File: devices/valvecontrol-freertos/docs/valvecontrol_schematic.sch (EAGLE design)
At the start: 38 parts, among them J1 M12-4PIN, J2 M12-4PIN, J3 PWR-3PIN, SW1 TACTILE, U1 nRF52832-QFAA, U2 RFM95C, U3 MCP2515-I/SO, U4 SN65HVD230DR, U5 FM25V02-G, U6 W25Q16JVSSIQ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

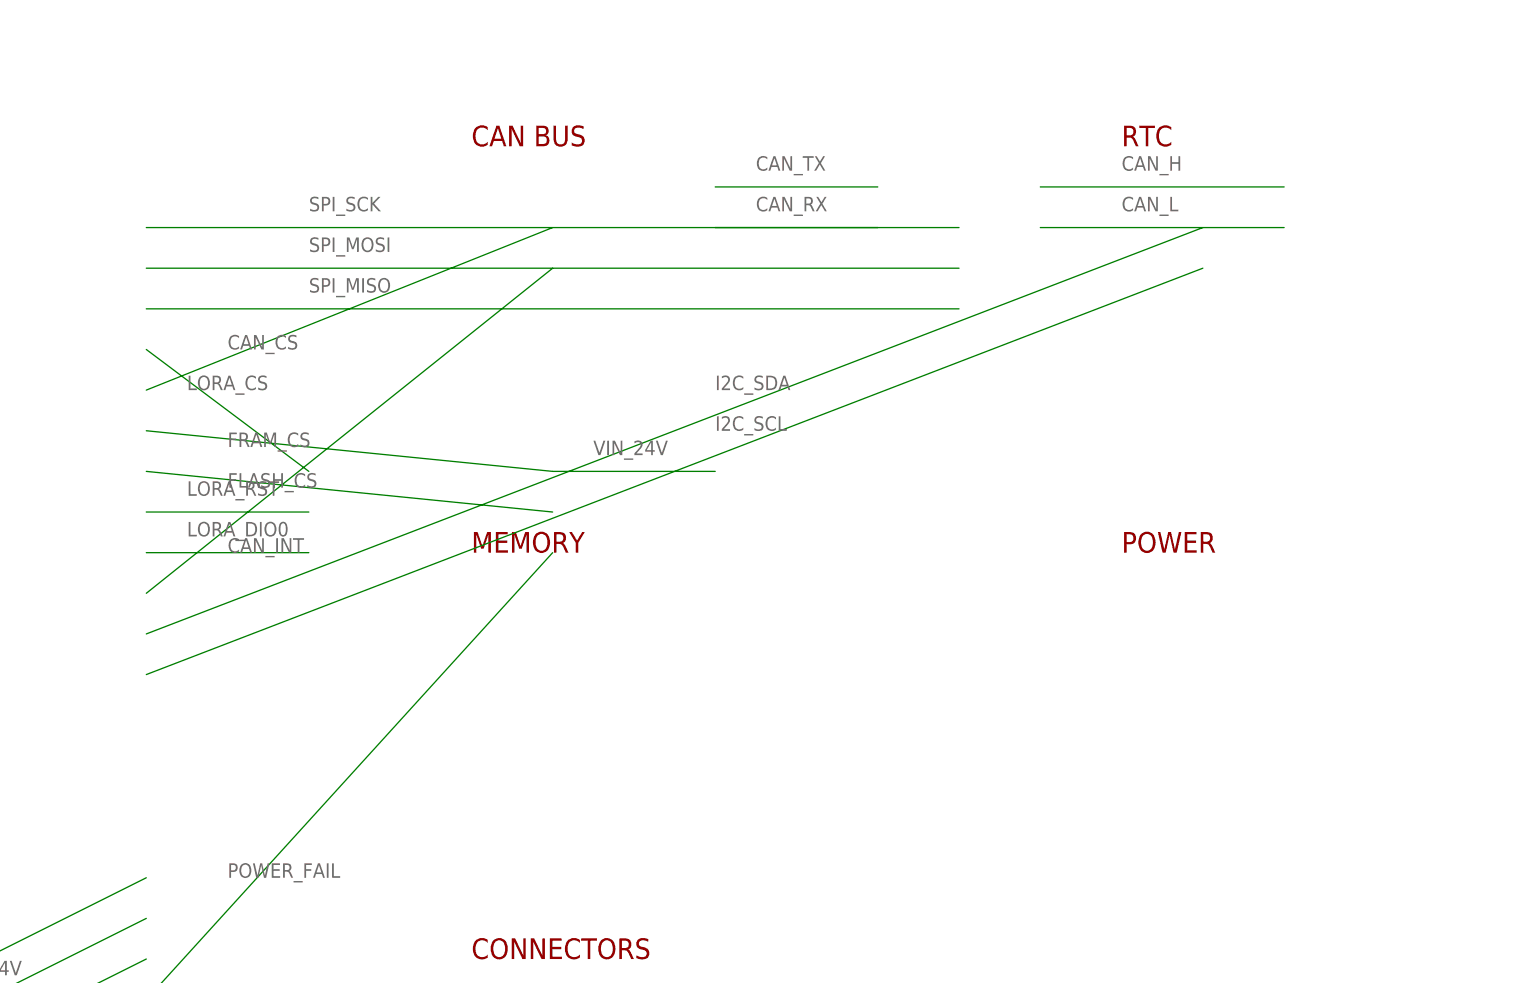
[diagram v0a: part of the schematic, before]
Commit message: So many little fixes to schematics, to board_config.h, to OTA, to flash ram, to moving logging back to FRAM device, to looking at how to make the devices last for 10+ years, to making sure BLE is integrated correctly.
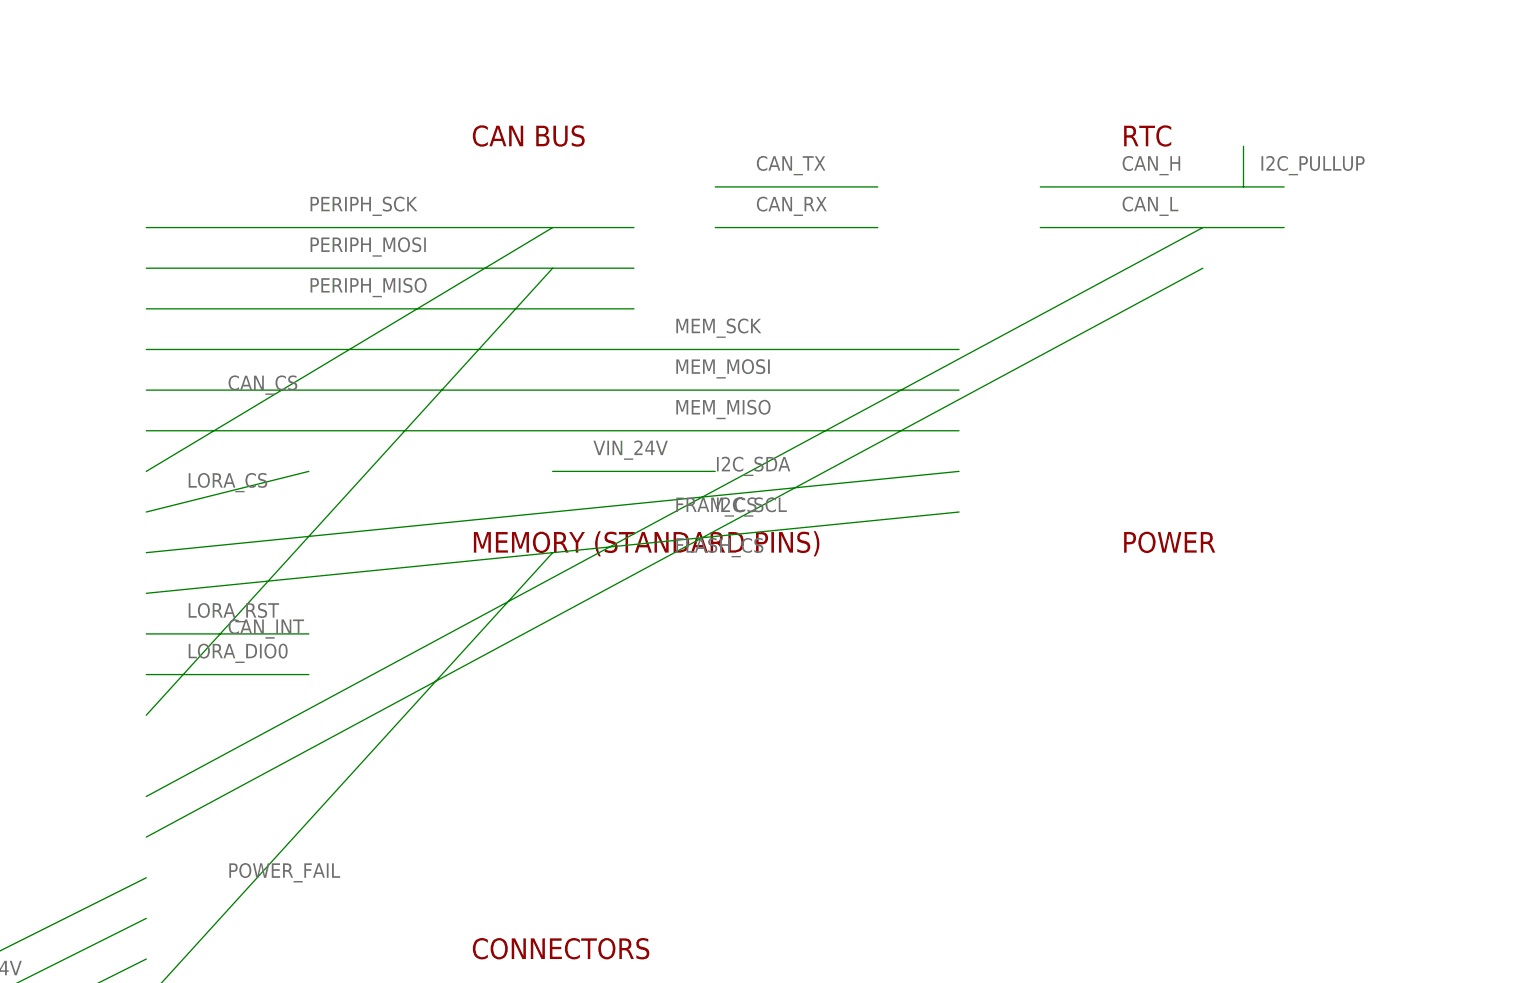
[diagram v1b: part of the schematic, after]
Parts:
- removed C12, C13, C14, C15: 100nF, None:0603
- added ANT1: 915MHz-WIRE, None:
- added C20, C21, C23, C30, C40, C41, C50, C51, C52, C60, C61: 100nF, None:0402
- added C22, C31: 10uF, None:0805
- added C24: 10nF, None:0402
- added C25: 1uF, None:0402
- added C32: 1.5pF, None:0402
- added C33: 1.2pF, None:0402
- added D1: PESD1CAN, None:SOT23
- added D2: SMBJ28A, None:SMB
- added D3, D4: PESD5V0S1BL, None:SOD323
- added F1: 500mA PTC, None:1206
- added L1: 10nH, None:0402
- added L2: 5.6nH, None:0402
- added Q1: SI2301CDS, None:SOT-23
- added R20, R21: 4.7K, None:0402
- added R22, R4, R5, R6: 10K, None:0402
- C1: value 10uF -> 10uF/50V
- C10, C11, C3, C4, C5, C6, C7, C8, C9, R1, R2, R3: device None:0603 -> None:0402
- SW1: device None:6MM -> None:6x6
- U2: value RFM95C -> RFM95C-915S2
- U5: value FM25V02-G -> MB85RS1MTPNF
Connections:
- removed net SPI_MISO: U1.P0.28, U2.MISO, U3.SO, U5.SO, U6.DO
- removed net SPI_MOSI: U1.P0.27, U2.MOSI, U3.SI, U5.SI, U6.DI
- removed net SPI_SCK: U1.P0.26, U2.SCK, U3.SCK, U5.SCK, U6.CLK
- new net I2C_PULLUP: R20.2, R21.2
- new net MEM_MISO: U1.P0.24, U5.SO, U6.DO
- new net MEM_MOSI: U1.P0.25, U5.SI, U6.DI
- new net MEM_SCK: U1.P0.26, U5.SCK, U6.CLK
- new net PERIPH_MISO: U1.P0.29, U2.MISO, U3.SO
- new net PERIPH_MOSI: U1.P0.28, U2.MOSI, U3.SI
- new net PERIPH_SCK: U1.P0.27, U2.SCK, U3.SCK
- net CAN_CS: now also U1.P0.30; no longer U1.P0.11
- net FLASH_CS: now also U1.P0.22; no longer U1.P0.29
- net FRAM_CS: now also U1.P0.23; no longer U1.P0.13
- net I2C_SCL: now also R21.1, U1.P0.03; no longer U1.P0.25
- net I2C_SDA: now also R20.1, U1.P0.02; no longer U1.P0.24
- net LORA_CS: now also U1.P0.31; no longer U1.P0.12
- net PAIRING_BTN: now also U1.P0.11; no longer U1.P0.30
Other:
- note added: "MEMORY (STANDARD PINS)"
- note removed: "MEMORY"

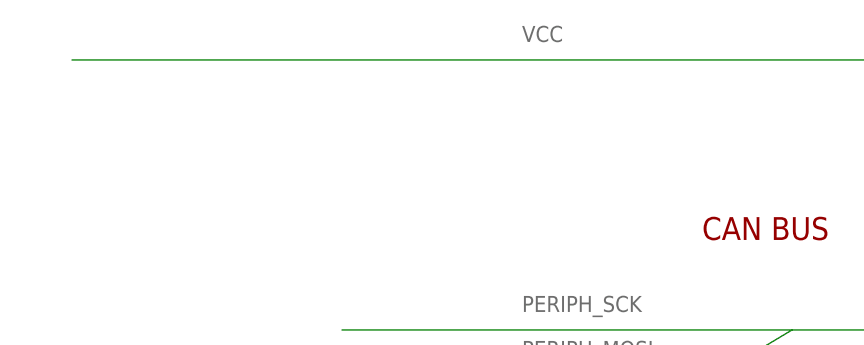
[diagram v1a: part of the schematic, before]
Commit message: renamed valve actuator directory to match the type valve support.  Added solenoid valve actuator
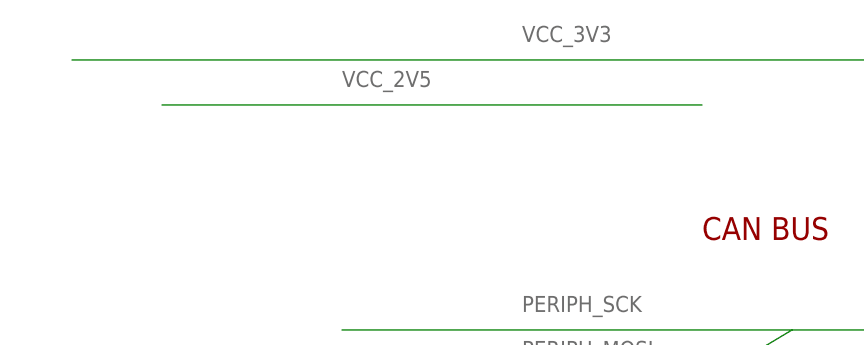
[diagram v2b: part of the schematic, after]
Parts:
- added C70, C71: 1uF, None:0402
- added U9: TLV73325PDBVR, None:SOT-23-5
- U8: value MCP1700-3302E -> AP2112K-3.3; device None:SOT-23 -> None:SOT-23-5
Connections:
- removed net VCC: U1.VDD, U2.VCC, U3.VDD, U4.VCC, U5.VCC, U6.VCC, U7.VDD, U8.VOUT
- new net VCC_2V5: C71.1, U1.VDD, U9.VOUT
- new net VCC_3V3: C70.1, U2.VCC, U3.VDD, U4.VCC, U5.VCC, U6.VCC, U7.VDD, U8.VOUT, U9.VIN
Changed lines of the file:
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@@
 <part name="R21" value="4.7K" device="0402"/>
 <!-- ================================================================== -->
-<!-- POWER - LDO (24V to 3.3V) -->
+<!-- POWER - LDO (24V to 3.3V) + LDO (3.3V to 2.5V) -->
 <!-- ================================================================== -->
-<part name="U8" value="MCP1700-3302E" device="SOT-23"/>
+<part name="U8" value="AP2112K-3.3" device="SOT-23-5"/>
 <part name="C1" value="10uF/50V" device="0805"/>
 <part name="C2" value="10uF" device="0805"/>
+<!-- LDO: 3.3V to 2.5V for MCU (low noise, low dropout) -->
+<part name="U9" value="TLV73325PDBVR" device="SOT-23-5"/>
+<part name="C70" value="1uF" device="0402"/>
+<part name="C71" value="1uF" device="0402"/>
 <!-- 24V Input Protection -->
 <part name="D2" value="SMBJ28A" device="SMB"/>
@@
 <!-- POWER NETS -->
 <!-- ================================================================== -->
-<!-- 3.3V Rail -->
-<net name="VCC" class="1">
+<!-- 3.3V Rail (from U8, powers LoRa, CAN, memory, RTC) -->
+<net name="VCC_3V3" class="1">
 <segment>
 <pinref part="U8" gate="G$1" pin="VOUT"/>
-<pinref part="U1" gate="G$1" pin="VDD"/>
+<pinref part="U9" gate="G$1" pin="VIN"/>
 <pinref part="U2" gate="G$1" pin="VCC"/>
 <pinref part="U3" gate="G$1" pin="VDD"/>
@@
 <pinref part="U6" gate="G$1" pin="VCC"/>
 <pinref part="U7" gate="G$1" pin="VDD"/>
+<pinref part="C70" gate="G$1" pin="1"/>
 <wire x1="50" y1="200" x2="200" y2="200" width="0.4064" layer="91"/>
 <label x="100" y="202" size="1.778" layer="95"/>
 </segment>
 </net>
+<!-- 2.5V Rail (from U9 LDO, powers MCU only) -->
+<net name="VCC_2V5" class="1">
+<segment>
+<pinref part="U9" gate="G$1" pin="VOUT"/>
+<pinref part="U1" gate="G$1" pin="VDD"/>
+<pinref part="C71" gate="G$1" pin="1"/>
+<wire x1="60" y1="195" x2="120" y2="195" width="0.4064" layer="91"/>
+<label x="80" y="197" size="1.778" layer="95"/>
+</segment>
+</net>
